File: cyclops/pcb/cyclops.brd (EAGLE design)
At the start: 124.5 x 79.9 mm, 183 parts, among them Q1 SSM3K324, Q2 SSM3K324, Q3 SSM3K324, Q4 IRF510, U1 MCP4921, U10 ADG1201, U11 THS4281, U12 MAX4564, U13 ZXTD, U14 ZXTD, U15 OPA1664, U2 LT1931, U3 LT1764A, U31 TPS62153, U4 BD00IA5WEFJ-E2, U5 TPS72325, U6 LT1711, U7 TLV3701, U8 ADR03, U9 LT1880

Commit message: Silkscreen work.
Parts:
- U4: value BD00IA5WEFJ-E2 -> BD00IA5WEFJ
- VPRE: device cyclops:TP16R -> jonnew:RC0603
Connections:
- removed net N$57: C24.2
- net GND: now also C24.2
- net VCTL: now also VPRE.1; no longer VPRE.TP
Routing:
- net -5V: track 32.7 -> 288.4 mm
- net GND: track 102.2 -> 100.9 mm, vias 259 -> 258
- net +6V: track 56.9 -> 58.2 mm, vias 28 -> 29
- net +13.3V: track 173.8 -> 173.0 mm

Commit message: Silkscreen nearly done. Final check and then time for fab.
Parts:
- removed C43: 22uF, jonnew:0805
- added C40: 22uF, cyclops:1210
- moved U$30 34.8 mm to (65.6, 24.6), turned to 315 degrees
- moved +5V 5.62 mm to (40.1, 27.8)
- moved U$60 4.49 mm to (90.4, 12.2)
- moved D2 0.76 mm to (30.7, 17.8)
- moved L5 0.76 mm to (34.9, 22.5)
- moved R2 0.76 mm to (25.4, 17.8)
- moved R3 0.76 mm to (25.4, 15.5)
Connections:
- net +5V: now also C40.1; no longer C43.1
- net GND: now also C40.2; no longer C43.2
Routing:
- net -5V: track 288.4 -> 36.3 mm
- net +5V: track 23.4 -> 21.5 mm
- net N$56: track 0.00 -> 1.68 mm
- net GND: track 100.9 -> 102.2 mm
- net +15V: track 51.6 -> 52.8 mm
- net TEENSY_VIN: track 20.1 -> 19.3 mm
- added copper zone on layer 1, net N$56
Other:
- board text added: "0"
- board text added: "0 Ohm"
- board text added: "1"
- board text added: "2"
- board text added: "3"
- board text added: "AUX"
- board text added: "BRD-ADDR"
- board text added: "CS"
- board text added: "CURR"
- board text added: "GAIN"
- board text added: "LDAC"
- board text added: "OC"
- board text added: "SENSE"
- board text added: "TEST"
- board text added: "TRIG"
- board text added: "VI"
- board text added: "ヽ(´ー｀)ノ"
- board text removed: "+12V"

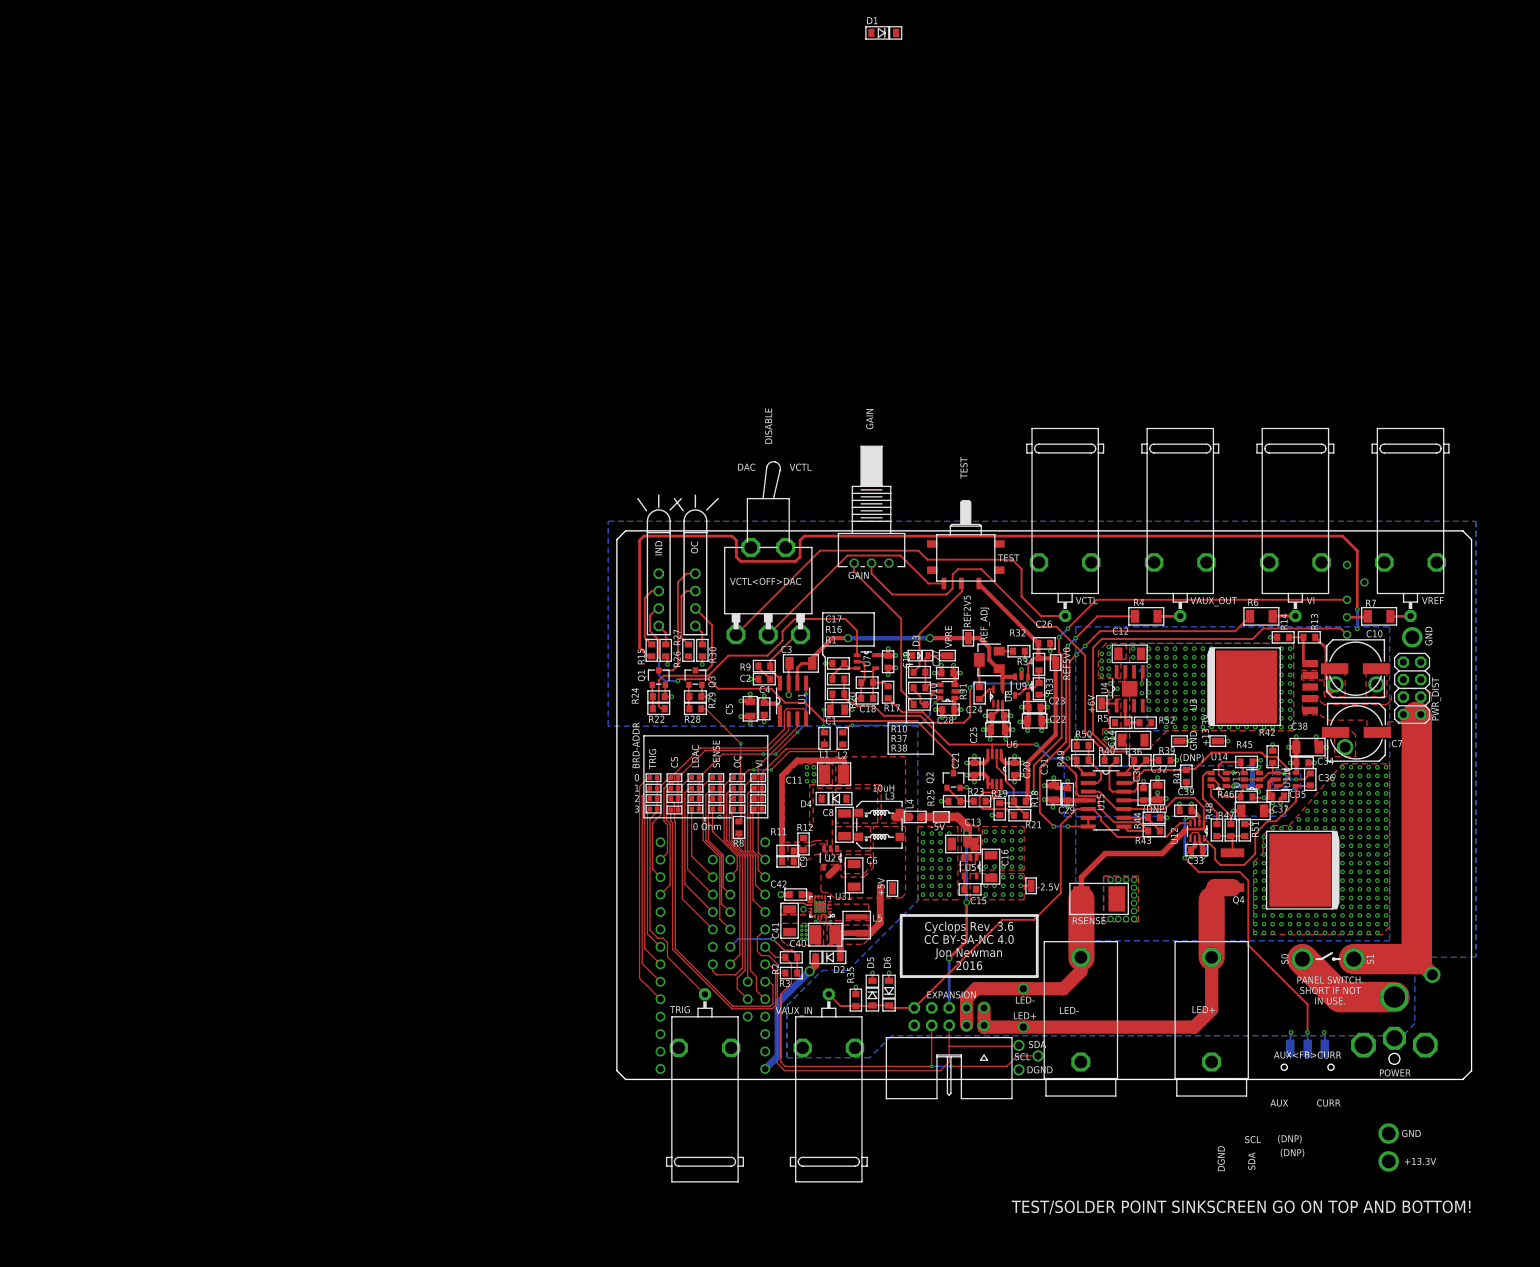
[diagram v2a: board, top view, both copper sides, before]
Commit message: Very close to finished with Rev. 3.6-beta PCB
- A couple lingering TODOs as stated on the first page of the schematic.
  Mostly mechnical/overlap issues at this point
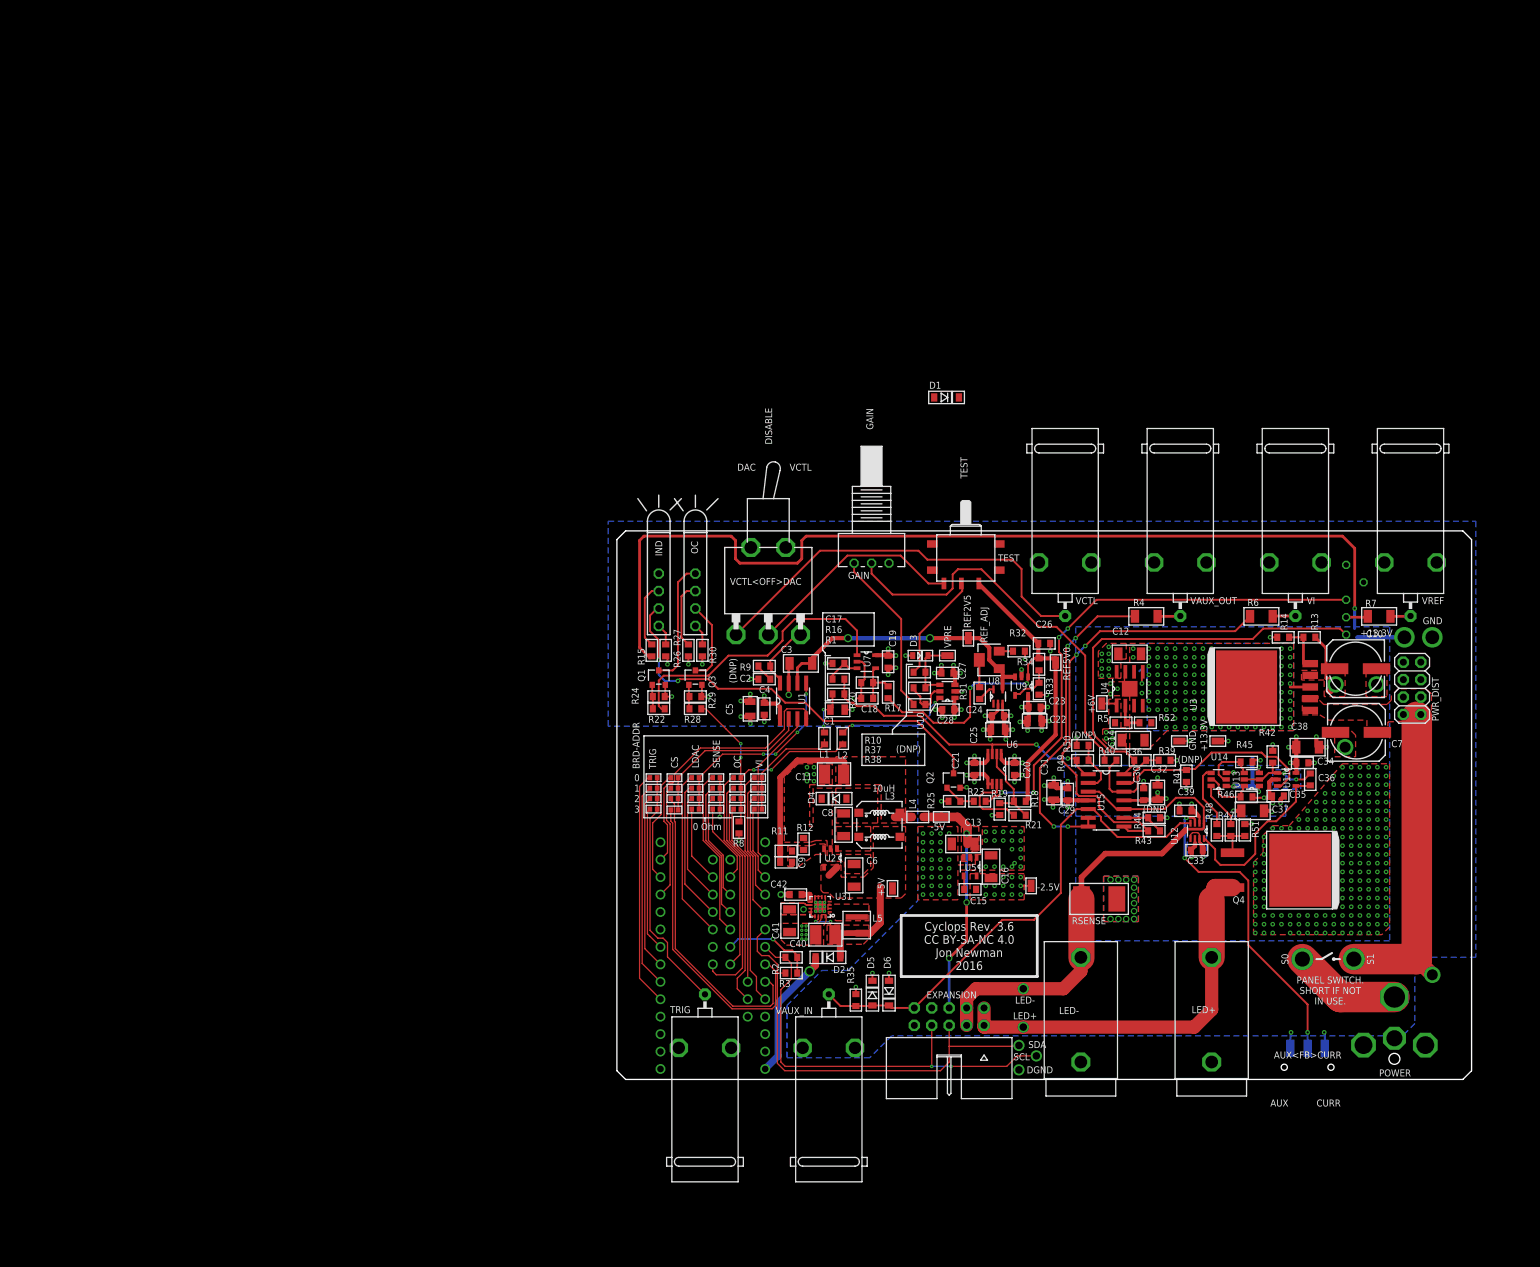
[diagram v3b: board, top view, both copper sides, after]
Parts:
- VREF<>TTL: value JS102 -> AS12AC
- moved D1 53.9 mm to (48.0, 99.3)
- moved L4 0.38 mm to (43.8, 38.2)
- moved C9 0.28 mm to (24.6, 31.6)
- moved R11 0.25 mm to (24.6, 33.3)
- moved C8 0.13 mm to (33.0, 37.1)
- moved VREF<>TTL 0.13 mm to (107.2, 64.8)
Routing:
- net +13.3V: track 173.0 -> 180.7 mm, vias 208 -> 207
- net GND: track 102.2 -> 106.9 mm, vias 258 -> 256
- net +6V: track 58.2 -> 59.4 mm, vias 29 -> 30
- net N$35: track 26.5 -> 27.1 mm
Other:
- board text removed: "TEST/SOLDER POINT SINKSCREEN GO ON TOP AND BOTTOM!"

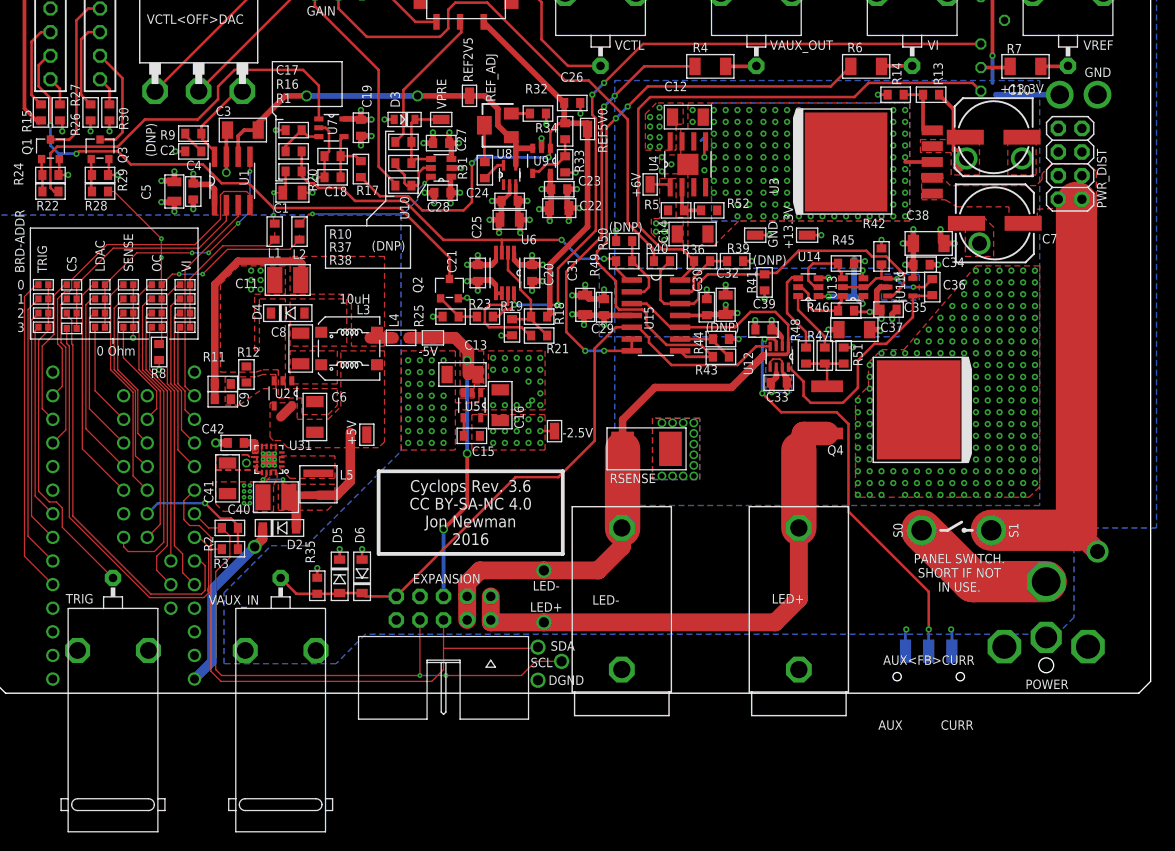
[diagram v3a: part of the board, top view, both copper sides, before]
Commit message: Fixed heatsink overlap issue and removed teensy AREF
- Moved to 1.7in x 1.7in heatsink because the AREF/TTL switch had a
  through hole contact that would have overlapped with the 1.8in
  version.
- Teensy AREF pin was in the way of the TRIG BNC and not needed, so I
  removed it. BOM has yet to be updated (3 pin header --> 2 pin).
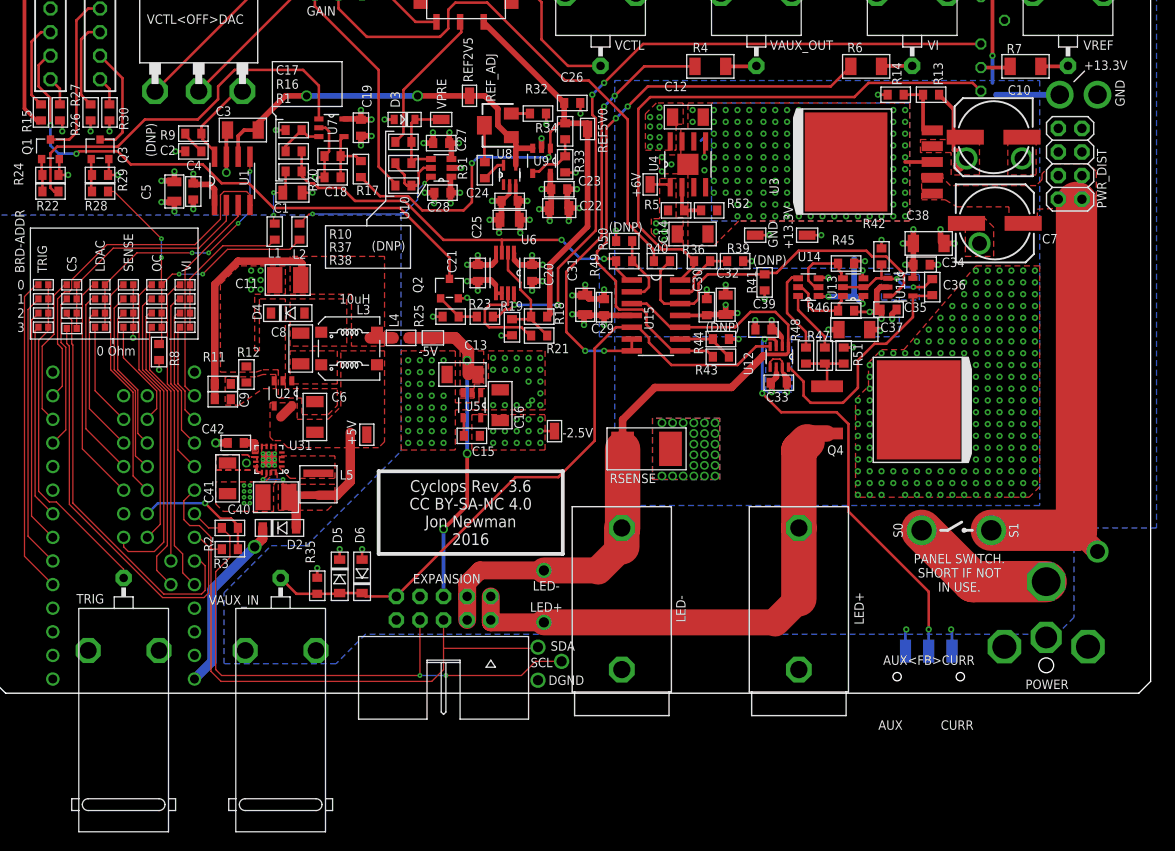
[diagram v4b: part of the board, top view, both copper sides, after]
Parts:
- HEATSINK: value BDN18 -> BDN17; device cyclops:BDN18 -> jonnew:BDN17
- moved TRIG 1.14 mm to (14.0, 0.00)
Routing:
- net VI: track 66.7 -> 62.9 mm
- net CS3: track 46.2 -> 45.4 mm
- net CS2: track 44.0 -> 43.2 mm
- net N$58: track 16.8 -> 16.1 mm
- net GND: vias 256 -> 268
